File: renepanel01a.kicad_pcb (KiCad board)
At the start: 2 copper layers, 172.4 x 128.5 mm, 63 parts, among them J1 Conn_01x12_Female, J2 Conn_01x12_Female, SW1 SW_Push_LED, SW10 SW_Push_LED, SW11 SW_Push_LED, SW12 SW_Push_LED, SW13 SW_Push_LED, SW14 SW_Push_LED, SW15 SW_Push_LED, SW16 SW_Push_LED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

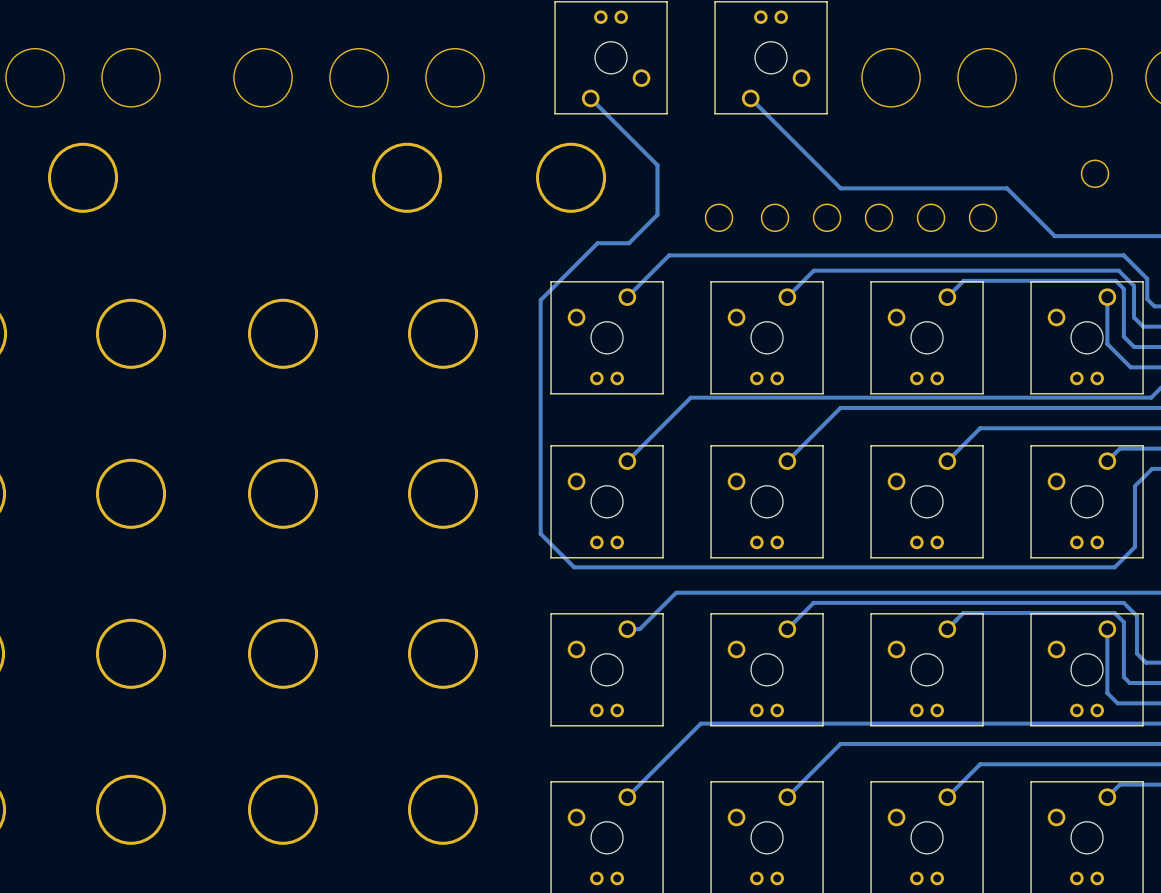
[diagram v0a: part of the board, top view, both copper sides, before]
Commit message: Add v1.1 panel.
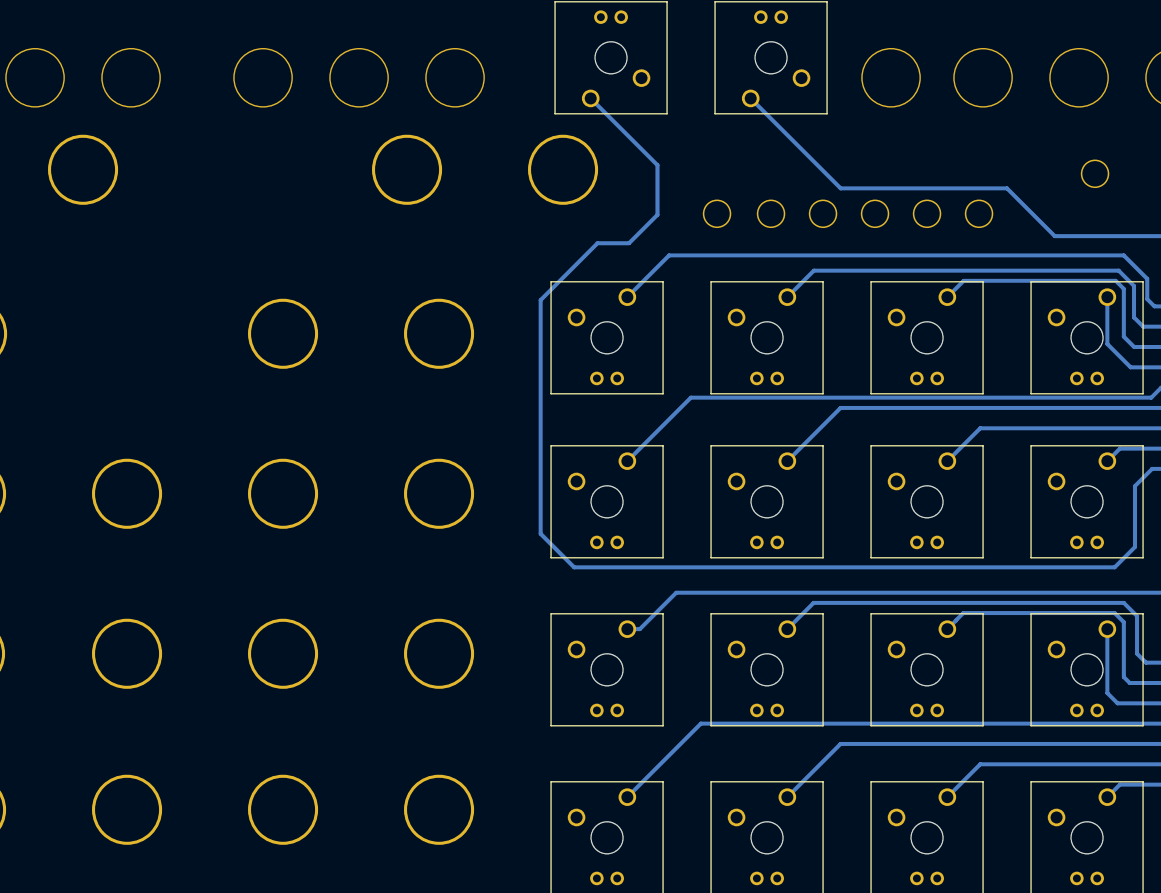
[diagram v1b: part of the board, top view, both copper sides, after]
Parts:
- removed the REF** at (34.2, -81.1)
- moved REF** 1.00 mm to (26.9, -101.1)
- moved REF** 0.50 mm to (68.6, -83.6)
- moved REF** 0.50 mm to (68.5, -62.5)
- moved REF** 0.50 mm to (33.6, -60.0)
- moved REF** 0.50 mm to (33.5, -38.8)
- moved REF** 0.50 mm to (68.3, -41.3)
- moved REF** 0.50 mm to (68.5, -21.1)
- moved REF** 0.50 mm to (33.6, -18.6)
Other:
- board text added: "make noise rene classic mechanical keyswitch panel v1.1 (unofficial) by ukyzky"
- board text removed: "make noise rene classic mechanical keyswitch panel v1.0 (unofficial) by ukyzky"
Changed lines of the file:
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@@
     (tracks 84)
     (zones 0)
-    (modules 63)
+    (modules 62)
     (nets 60)
   )
@@
   )
   (setup
-    (last_trace_width 0.5)
+    (last_trace_width 0.25)
     (user_trace_width 0.5)
     (trace_clearance 0.2)
@@
       (drillshape 0)
       (scaleselection 1)
-      (outputdirectory "./renepanel01a"))
+      (outputdirectory "./renepanel01b"))
   )
   (net 0 "")
@@
     (fp_line (start -0.508 0) (end 0.508 0) (layer F.Fab) (width 0.15))
     (fp_line (start 0 -0.508) (end 0 0.508) (layer F.Fab) (width 0.15))
-    (pad 1 thru_hole circle (at -7.716 11.172 90) (size 3.556 3.556) (drill 3.175) (layers *.Cu *.Mask))
+    (pad 1 thru_hole circle (at -8.216 10.672 90) (size 3.556 3.556) (drill 3.175) (layers *.Cu *.Mask))
   )
   (module 4ms_Faceplate:Faceplate_Hole_Rail_Hole (layer F.Cu)
@@
     (fp_line (start 0 -0.508) (end 0 0.508) (layer F.Fab) (width 0.15))
     (fp_line (start -0.508 0) (end 0.508 0) (layer F.Fab) (width 0.15))
-    (pad 1 thru_hole circle (at -9.979 6.092 90) (size 3.556 3.556) (drill 3.175) (layers *.Cu *.Mask))
+    (pad 1 thru_hole circle (at -10.479 5.592 90) (size 3.556 3.556) (drill 3.175) (layers *.Cu *.Mask))
   )
   (module 4ms_Faceplate:Faceplate_Hole_Rail_Hole (layer F.Cu)
@@
     (fp_line (start -0.508 0) (end 0.508 0) (layer F.Fab) (width 0.15))
     (fp_line (start 0 -0.508) (end 0 0.508) (layer F.Fab) (width 0.15))
-    (pad 1 thru_hole circle (at -9.009 6.092 90) (size 3.556 3.556) (drill 3.175) (layers *.Cu *.Mask))
+    (pad 1 thru_hole circle (at -9.509 5.592 90) (size 3.556 3.556) (drill 3.175) (layers *.Cu *.Mask))
   )
   (module 4ms_Faceplate:Faceplate_Hole_Rail_Hole (layer F.Cu)
@@
     (fp_line (start 0 -0.508) (end 0 0.508) (layer F.Fab) (width 0.15))
     (fp_line (start -0.508 0) (end 0.508 0) (layer F.Fab) (width 0.15))
-    (pad 1 thru_hole circle (at -6.746 11.172 90) (size 3.556 3.556) (drill 3.175) (layers *.Cu *.Mask))
+    (pad 1 thru_hole circle (at -7.246 10.672 90) (size 3.556 3.556) (drill 3.175) (layers *.Cu *.Mask))
   )
   (module 4ms_Faceplate:Faceplate_Hole_Pot_9mm_Metal_Collar (layer F.Cu)
@@
     (fp_line (start 0 -0.508) (end 0 0.508) (layer F.Fab) (width 0.15))
     (fp_line (start -0.508 0) (end 0.508 0) (layer F.Fab) (width 0.15))
-    (pad 1 thru_hole circle (at -15.64 4.213) (size 7.45 7.45) (drill 7.1) (layers *.Cu *.Mask))
+    (pad 1 thru_hole circle (at -16.14 4.213) (size 7.45 7.45) (drill 7.1) (layers *.Cu *.Mask))
   )
   (module 4ms_Faceplate:Faceplate_Hole_Pot_9mm_Metal_Collar (layer F.Cu)
@@
     (fp_line (start -0.508 0) (end 0.508 0) (layer F.Fab) (width 0.15))
     (fp_line (start 0 -0.508) (end 0 0.508) (layer F.Fab) (width 0.15))
-    (pad 1 thru_hole circle (at -15.448 6.499) (size 7.45 7.45) (drill 7.1) (layers *.Cu *.Mask))
+    (pad 1 thru_hole circle (at -15.948 6.499) (size 7.45 7.45) (drill 7.1) (layers *.Cu *.Mask))
   )
   (module 4ms_Faceplate:Faceplate_Hole_Pot_9mm_Metal_Collar (layer F.Cu)
@@
     (fp_line (start 0 -0.508) (end 0 0.508) (layer F.Fab) (width 0.15))
     (fp_line (start -0.508 0) (end 0.508 0) (layer F.Fab) (width 0.15))
-    (pad 1 thru_hole circle (at 16.943 2.057) (size 8.762 8.762) (drill 8) (layers *.Cu *.Mask))
+    (pad 1 thru_hole circle (at 15.943 1.057) (size 8.762 8.762) (drill 8) (layers *.Cu *.Mask))
   )
   (module 4ms_Faceplate:Faceplate_Hole_Pot_16mm_Hole8mm (layer F.Cu)
@@
     (fp_line (start -0.508 0) (end 0.508 0) (layer F.Fab) (width 0.15))
     (fp_line (start 0 -0.508) (end 0 0.508) (layer F.Fab) (width 0.15))
-    (pad 1 thru_hole circle (at 10.604 2.235) (size 8.762 8.762) (drill 8) (layers *.Cu *.Mask))
-  )
-  (module 4ms_Faceplate:Faceplate_Hole_Pot_16mm_Hole8mm (layer F.Cu)
-    (at 26.878 -100.094)
+    (pad 1 thru_hole circle (at 10.604 1.235) (size 8.762 8.762) (drill 8) (layers *.Cu *.Mask))
+  )
+  (module 4ms_Faceplate:Faceplate_Hole_Pot_16mm_Hole8mm (layer F.Cu)
+    (at 26.878 -101.094)
     (fp_text reference REF** (at 0.254 2.286) (layer F.SilkS) hide
       (effects (font (size 1 1) (thickness 0.15)))
@@
   )
   (module 4ms_Faceplate:Faceplate_Hole_Pot_16mm_Hole8mm (layer F.Cu)
-    (at 34.244 -81.108)
-    (fp_text reference REF** (at 0.254 2.286) (layer F.SilkS) hide
-      (effects (font (size 1 1) (thickness 0.15)))
-    )
-    (fp_text value Faceplate_Hole_Pot_16mm_Hole8mm (at 0.58 4.95) (layer F.Fab) hide
-      (effects (font (size 1 1) (thickness 0.15)))
-    )
-    (fp_line (start 0 -0.508) (end 0 0.508) (layer F.Fab) (width 0.15))
-    (fp_line (start -0.508 0) (end 0.508 0) (layer F.Fab) (width 0.15))
-    (pad 1 thru_hole circle (at -1.244 0.608) (size 8.762 8.762) (drill 8) (layers *.Cu *.Mask))
-  )
-  (module 4ms_Faceplate:Faceplate_Hole_Pot_16mm_Hole8mm (layer F.Cu)
     (at 16.764 -80.01)
     (fp_text reference REF** (at 0.254 2.286) (layer F.SilkS) hide
@@
   )
   (module 4ms_Faceplate:Faceplate_Hole_Pot_16mm_Hole8mm (layer F.Cu)
-    (at 69.088 -83.566)
+    (at 68.588 -83.566)
     (fp_text reference REF** (at 0.254 2.286) (layer F.SilkS) hide
       (effects (font (size 1 1) (thickness 0.15)))
@@
   )
   (module 4ms_Faceplate:Faceplate_Hole_Pot_16mm_Hole8mm (layer F.Cu)
-    (at 68.961 -62.484)
+    (at 68.461 -62.484)
     (fp_text reference REF** (at 0.254 2.286) (layer F.SilkS) hide
       (effects (font (size 1 1) (thickness 0.15)))
@@
   )
   (module 4ms_Faceplate:Faceplate_Hole_Pot_16mm_Hole8mm (layer F.Cu)
-    (at 34.117 -60.026)
+    (at 33.617 -60.026)
     (fp_text reference REF** (at 0.254 2.286) (layer F.SilkS) hide
       (effects (font (size 1 1) (thickness 0.15)))
@@
   )
   (module 4ms_Faceplate:Faceplate_Hole_Pot_16mm_Hole8mm (layer F.Cu)
-    (at 33.99 -38.817)
+    (at 33.49 -38.817)
     (fp_text reference REF** (at 0.254 2.286) (layer F.SilkS) hide
       (effects (font (size 1 1) (thickness 0.15)))
@@
   )
   (module 4ms_Faceplate:Faceplate_Hole_Pot_16mm_Hole8mm (layer F.Cu)
-    (at 68.834 -41.275)
+    (at 68.334 -41.275)
     (fp_text reference REF** (at 0.254 2.286) (layer F.SilkS) hide
       (effects (font (size 1 1) (thickness 0.15)))
@@
   )
   (module 4ms_Faceplate:Faceplate_Hole_Pot_16mm_Hole8mm (layer F.Cu)
-    (at 68.961 -21.082)
+    (at 68.461 -21.082)
     (fp_text reference REF** (at 0.254 2.286) (layer F.SilkS) hide
       (effects (font (size 1 1) (thickness 0.15)))
@@
   )
   (module 4ms_Faceplate:Faceplate_Hole_Pot_16mm_Hole8mm (layer F.Cu)
-    (at 34.117 -18.624)
+    (at 33.617 -18.624)
     (fp_text reference REF** (at 0.254 2.286) (layer F.SilkS) hide
       (effects (font (size 1 1) (thickness 0.15)))
@@
     (fp_line (start 0 -0.508) (end 0 0.508) (layer F.Fab) (width 0.15))
     (fp_line (start -0.508 0) (end 0.508 0) (layer F.Fab) (width 0.15))
-    (pad 1 thru_hole circle (at -7.404 6.219 90) (size 3.556 3.556) (drill 3.175) (layers *.Cu *.Mask))
+    (pad 1 thru_hole circle (at -7.904 5.719 90) (size 3.556 3.556) (drill 3.175) (layers *.Cu *.Mask))
   )
   (module 4ms_Faceplate:Faceplate_Hole_Rail_Hole (layer F.Cu)
@@
     (fp_line (start -0.508 0) (end 0.508 0) (layer F.Fab) (width 0.15))
     (fp_line (start 0 -0.508) (end 0 0.508) (layer F.Fab) (width 0.15))
-    (pad 1 thru_hole circle (at -5.641 11.299 90) (size 3.556 3.556) (drill 3.175) (layers *.Cu *.Mask))
+    (pad 1 thru_hole circle (at -5.891 10.799 90) (size 3.556 3.556) (drill 3.175) (layers *.Cu *.Mask))
   )
   (module 4ms_Faceplate:Faceplate_Rail_Mount_Slot_Plated (layer F.Cu)
@@
     (pad "" np_thru_hole circle (at 0 0) (size 4 4) (drill 4) (layers *.Cu *.Mask))
   )
-  (gr_text "make noise rene classic mechanical keyswitch panel v1.0 (unofficial) by ukyzky" (at 2.921 -55.753 90) (layer B.SilkS)
+  (gr_text "make noise rene classic mechanical keyswitch panel v1.1 (unofficial) by ukyzky" (at 2.921 -55.753 90) (layer B.SilkS)
     (effects (font (size 1 1) (thickness 0.15)) (justify mirror))
   )
